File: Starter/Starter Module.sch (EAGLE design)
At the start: 3 parts

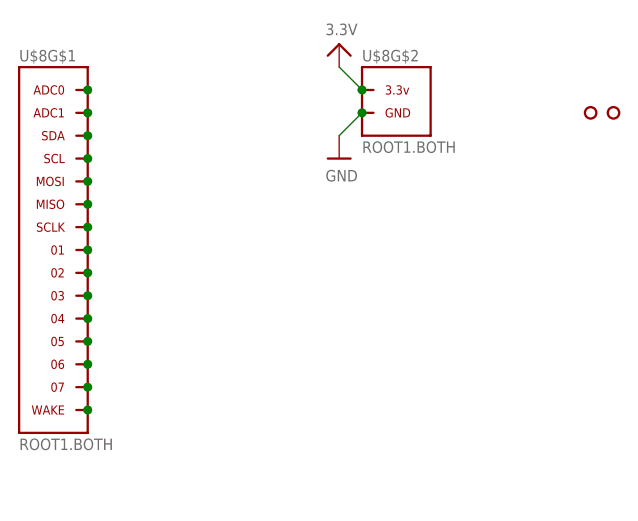
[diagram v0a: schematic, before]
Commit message: Updated Starter Module with standard silkscreen and included all libraries.
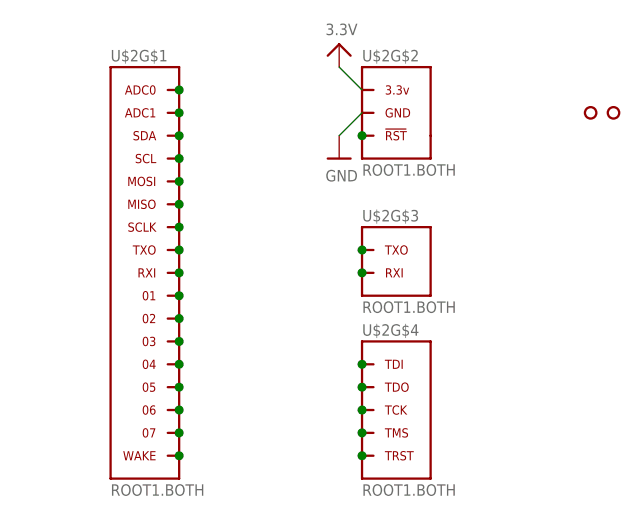
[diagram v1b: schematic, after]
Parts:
- removed U$8: ROOT1.BOTH, thinkmaketest:ROOT1.BOTH
- added U$2: ROOT1.BOTH, thinkmaketest:ROOT1.BOTH
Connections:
- new net N$16: U$2G$1.07
- new net N$17: U$2G$1.WAKE
- new net N$18: U$2G$4.TDI
- new net N$19: U$2G$4.TDO
- new net N$20: U$2G$4.TCK
- new net N$21: U$2G$4.TMS
- new net N$22: U$2G$4.TRST
- new net N$23: U$2G$3.RXI
- new net N$24: U$2G$3.TXO
- new net N$25: U$2G$2.!RST
- net 3.3V: now also U$2G$2.3.3V; no longer U$8G$2.3.3V
- net GND: now also U$2G$2.GND; no longer U$8G$2.GND
- net N$1: now also U$2G$1.04; no longer U$8G$1.ADC0
- net N$10: now also U$2G$1.01; no longer U$8G$1.03
- net N$11: now also U$2G$1.02; no longer U$8G$1.04
- net N$12: now also U$2G$1.MOSI; no longer U$8G$1.05
- net N$13: now also U$2G$1.ADC0; no longer U$8G$1.06
- net N$14: now also U$2G$1.05; no longer U$8G$1.07
- net N$15: now also U$2G$1.06; no longer U$8G$1.WAKE
- net N$2: now also U$2G$1.ADC1; no longer U$8G$1.ADC1
- net N$3: now also U$2G$1.SDA; no longer U$8G$1.SDA
- net N$4: now also U$2G$1.SCL; no longer U$8G$1.SCL
- net N$5: now also U$2G$1.03; no longer U$8G$1.MOSI
- net N$6: now also U$2G$1.MISO; no longer U$8G$1.MISO
- net N$7: now also U$2G$1.SCLK; no longer U$8G$1.SCLK
- net N$8: now also U$2G$1.TXO; no longer U$8G$1.01
- net N$9: now also U$2G$1.RXI; no longer U$8G$1.02
